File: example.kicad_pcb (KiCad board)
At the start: 2 copper layers, 127 x 101.6 mm, 16 parts, among them P1 CONN_01X03, P3 CONN_01X06, P4 CONN_01X01, P6 CONN_01X12, P7 CONN_01X16, P8 CONN_01X09

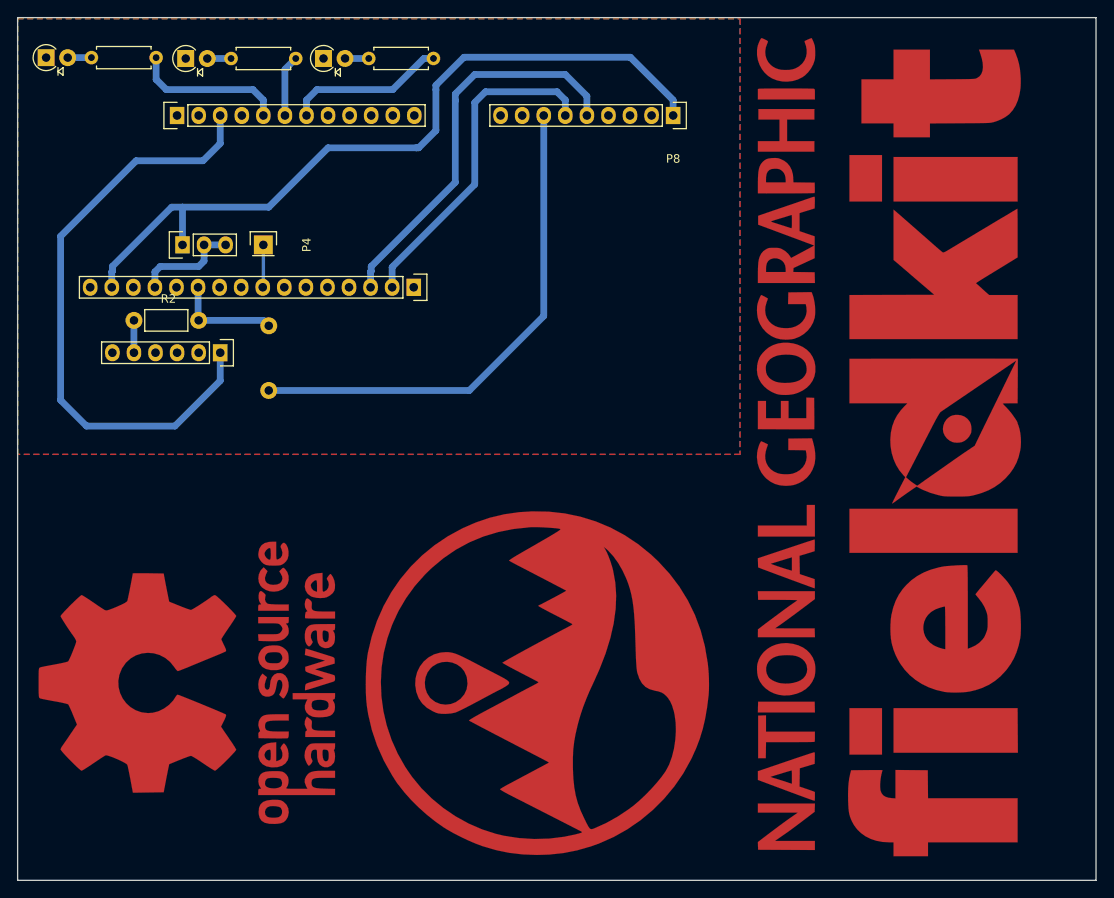
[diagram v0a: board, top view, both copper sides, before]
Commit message: Add a hole to feed the battery cable through.
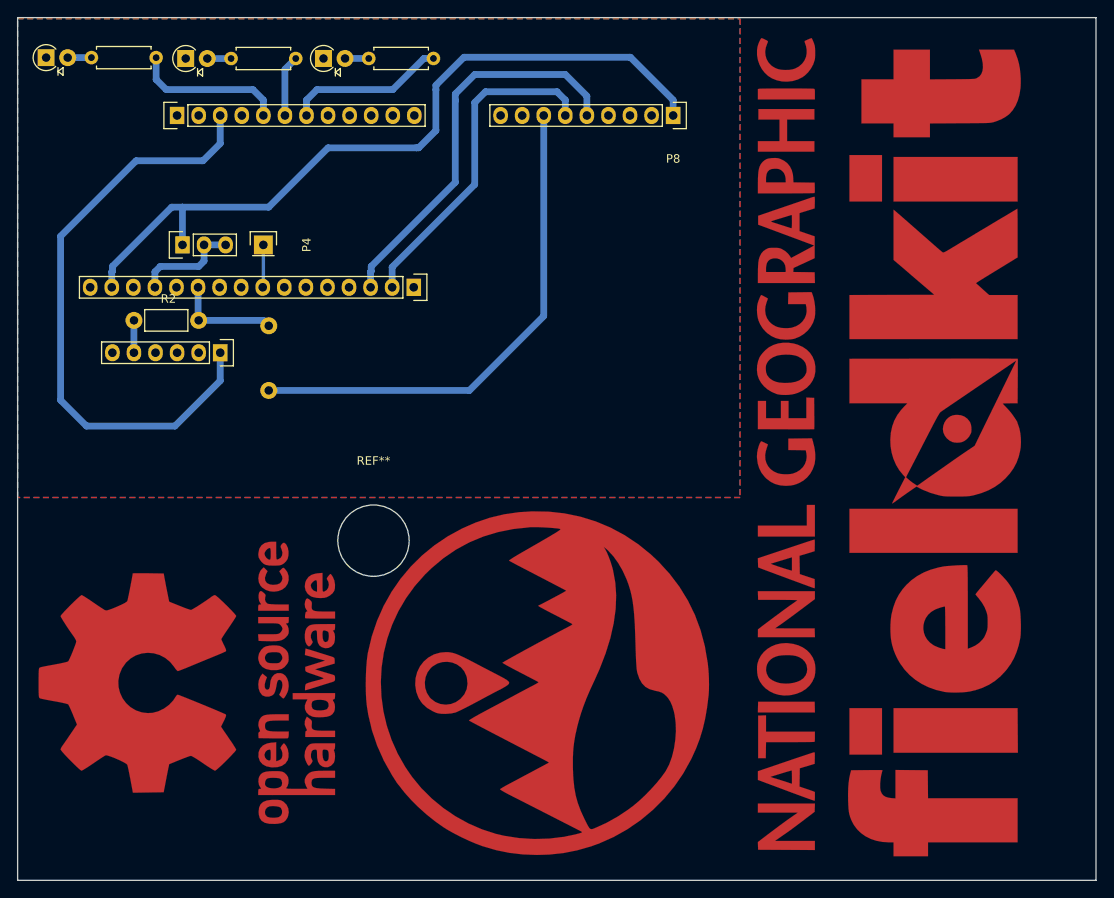
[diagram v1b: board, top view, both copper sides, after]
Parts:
- added REF**: MountingHole_8.4mm_M8, Mounting_Holes:MountingHole_8.4mm_M8, F.Cu at (152.4, 106.7)
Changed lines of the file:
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@@
 (kicad_pcb (version 4) (host pcbnew 4.0.6)
   (general
-    (links 24)
+    (links 0)
     (no_connects 0)
     (area 110.414999 45.009999 237.565001 146.760001)
@@
     (tracks 75)
     (zones 0)
-    (modules 16)
+    (modules 17)
     (nets 15)
   )
@@
     )
   )
+  (module Mounting_Holes:MountingHole_8.4mm_M8 (layer F.Cu)
+    (at 152.4 106.68)
+    (descr "Mounting Hole 8.4mm, no annular, M8")
+    (tags "mounting hole 8.4mm no annular m8")
+    (fp_text reference REF** (at 0 -9.4) (layer F.SilkS)
+      (effects (font (size 1 1) (thickness 0.15)))
+    )
+    (fp_text value MountingHole_8.4mm_M8 (at 0 9.4) (layer F.Fab)
+      (effects (font (size 1 1) (thickness 0.15)))
+    )
+    (fp_circle (center 0 0) (end 8.4 0) (layer Cmts.User) (width 0.15))
+    (fp_circle (center 0 0) (end 8.65 0) (layer F.CrtYd) (width 0.05))
+    (pad 1 np_thru_hole circle (at 0 0) (size 8.4 8.4) (drill 8.4) (layers *.Cu *.Mask))
+  )
   (gr_line (start 110.49 146.685) (end 237.49 146.685) (angle 90) (layer Edge.Cuts) (width 0.15))
   (gr_line (start 237.49 45.085) (end 237.49 146.685) (angle 90) (layer Edge.Cuts) (width 0.15))
@@
     (polygon
       (pts
-        (xy 110.49 45.212) (xy 195.58 45.212) (xy 195.58 96.52) (xy 110.49 96.52)
+        (xy 110.49 45.212) (xy 195.58 45.212) (xy 195.58 101.6) (xy 110.49 101.6)
       )
     )
@@
     (polygon
       (pts
-        (xy 110.49 45.212) (xy 195.58 45.212) (xy 195.58 96.52) (xy 110.49 96.52)
+        (xy 110.49 45.212) (xy 195.58 45.212) (xy 195.58 101.6) (xy 110.49 101.6)
       )
     )

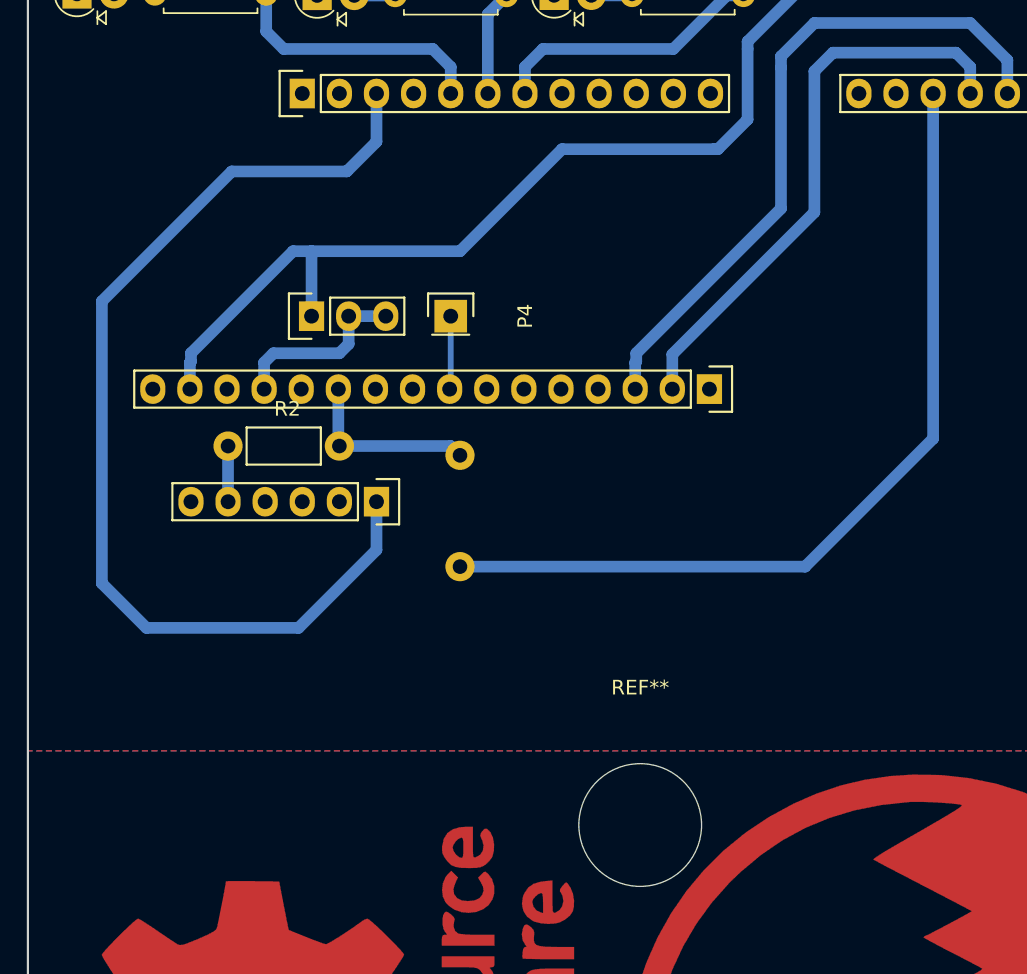
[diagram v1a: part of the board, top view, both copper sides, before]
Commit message: Drop the charging board, it's unnecessary. Make sensor a legit conn.
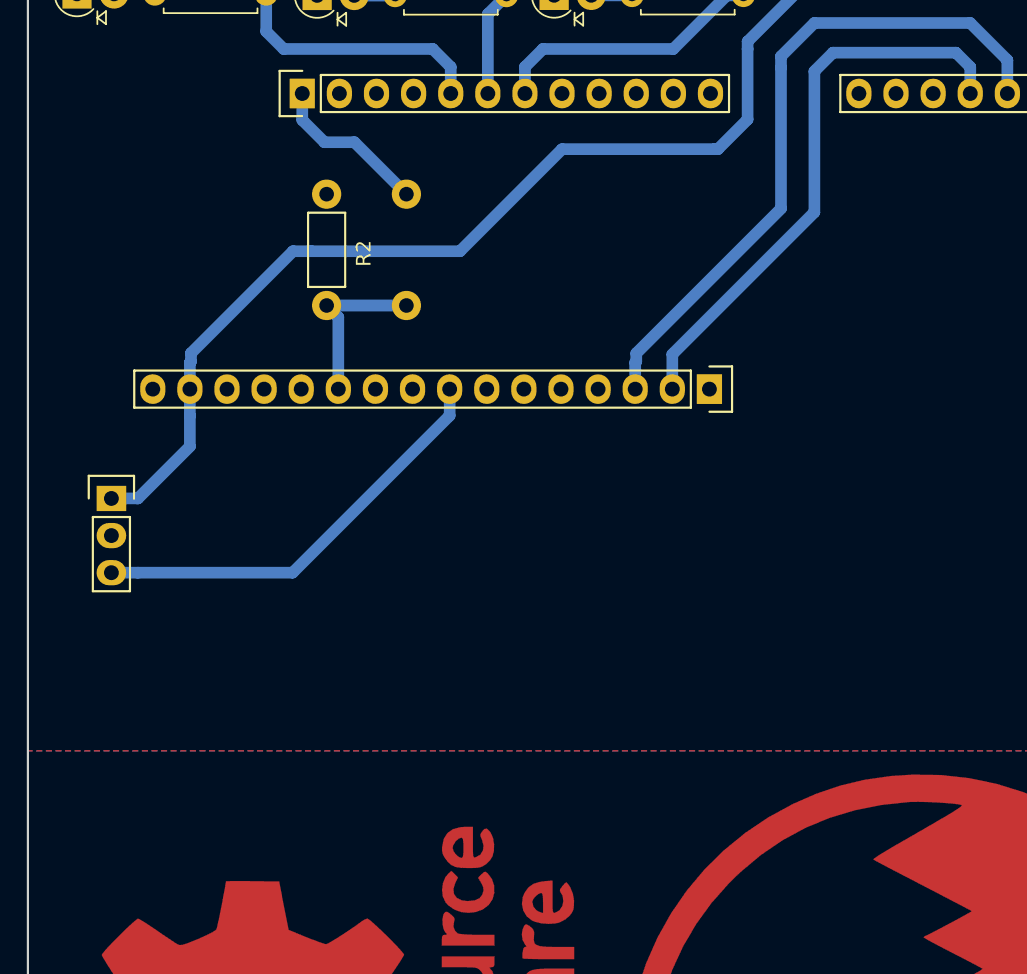
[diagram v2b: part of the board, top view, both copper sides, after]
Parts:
- removed P3: CONN_01X06, Socket_Strips:Socket_Strip_Straight_1x06
- removed P4: CONN_01X01, Socket_Strips:Socket_Strip_Straight_1x01
- removed REF**: MountingHole_8.4mm_M8, Mounting_Holes:MountingHole_8.4mm_M8
- moved P1 18.5 mm to (116.2, 84.3), turned to 270 degrees
- moved R2 18.5 mm to (130.9, 63.5), turned to 270 degrees
- moved R1 10.9 mm to (136.4, 71.1), turned to 90 degrees
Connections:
- P1 pad 3: GND -> Net-(P1-Pad3)
- P6 pad 1: (no net) -> Net-(P6-Pad1)
- P6 pad 10: (no net) -> Net-(P6-Pad10)
- P6 pad 11: (no net) -> Net-(P6-Pad11)
- P6 pad 12: (no net) -> Net-(P6-Pad12)
- P6 pad 2: (no net) -> Net-(P6-Pad2)
- P6 pad 3: /LOAD -> Net-(P6-Pad3)
- P6 pad 4: (no net) -> Net-(P6-Pad4)
- P6 pad 8: (no net) -> Net-(P6-Pad8)
- P6 pad 9: (no net) -> Net-(P6-Pad9)
- P7 pad 1: (no net) -> Net-(P7-Pad1)
- P7 pad 10: (no net) -> Net-(P7-Pad10)
- P7 pad 12: (no net) -> Net-(P7-Pad12)
- P7 pad 14: (no net) -> Net-(P7-Pad14)
- P7 pad 16: (no net) -> Net-(P7-Pad16)
- P7 pad 4: (no net) -> Net-(P7-Pad4)
- P7 pad 5: (no net) -> Net-(P7-Pad5)
- P7 pad 6: (no net) -> Net-(P7-Pad6)
- P7 pad 7: (no net) -> Net-(P7-Pad7)
- P7 pad 8: Net-(P4-Pad1) -> Net-(P1-Pad3)
- P7 pad 9: (no net) -> Net-(P7-Pad9)
- P8 pad 2: (no net) -> Net-(P8-Pad2)
- P8 pad 3: (no net) -> Net-(P8-Pad3)
- P8 pad 4: (no net) -> Net-(P8-Pad4)
- P8 pad 8: (no net) -> Net-(P8-Pad8)
- P8 pad 9: (no net) -> Net-(P8-Pad9)
- R1 pad 2: GND -> Net-(P6-Pad1)
- R2 pad 1: Net-(P3-Pad5) -> GND
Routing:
- net GND: track 72.2 -> 0.00 mm
- net /LOAD: track 71.5 -> 0.00 mm
- net Net-(P1-Pad3): track 0.00 -> 29.5 mm
- net Net-(P6-Pad1): track 0.00 -> 11.0 mm
- net /3V3: track 90.2 -> 96.5 mm
- net Net-(P4-Pad1): track 5.02 -> 0.00 mm
- net Net-(P3-Pad5): track 3.81 -> 0.00 mm
- net /BAT: track 12.4 -> 11.5 mm
